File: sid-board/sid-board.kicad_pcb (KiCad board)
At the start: 2 copper layers, 13 parts, among them J1 ICM_CONN, J2 SID_CONN, J3 5V/GND, J4 3.3V/GND, J5 SPI, J6 UARTAB/IRQ, U1 SC16IS752IPW, U2 LM2596MODULE, U3 PCA82C250, U4 PCA82C250

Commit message: Happy with first prototype, going to try get it made!
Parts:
- J1, J2: footprint Connector_PinHeader_2.54mm:PinHeader_2x06_P2.54mm_Vertical -> sid-board:SAAB_SID_CONNECTOR_HEADER
- J3: value 5V/GND -> 5V OUT
- J4: value 3.3V/GND -> 3.3V IN
- J6: value UARTAB/IRQ -> UARTA/UARTB/IRQ
- U1: value SC16IS752IPW -> SC16IS752
- moved J3 14.3 mm to (92.6, 123.8)
- moved J6 14.2 mm to (81.2, 112.5)
- moved C2 12.2 mm to (87.0, 78.9), turned to 90 degrees
- moved U1 11.7 mm to (73.7, 112.4), turned to 180 degrees
- moved SPI 10.7 mm to (102.1, 123.4)
- moved J1 10.2 mm to (94.0, 66.0), turned to 0 degrees
- moved C1 9.02 mm to (80.0, 78.9), turned to 90 degrees
- moved U4 8.90 mm to (73.7, 76.2)
- moved R1 7.79 mm to (66.0, 108.3)
- moved J2 6.35 mm to (73.7, 66.0), turned to 0 degrees
- moved U2 5.08 mm to (83.8, 94.0)
- moved U3 4.84 mm to (93.3, 76.2)
- moved J4 4.27 mm to (83.8, 123.8)
- renumbered J5 to SPI
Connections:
- U3 pad 4: (no net) -> Net-(J6-Pad1)
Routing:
- net GND: track 0.00 -> 188.3 mm, vias 0 -> 3
- net VDD_5V: track 0.00 -> 78.5 mm, vias 0 -> 1
- net Net-(J6-Pad4): track 0.00 -> 64.5 mm
- net Net-(J6-Pad3): track 0.00 -> 61.5 mm
- net Net-(J6-Pad2): track 0.00 -> 49.5 mm, vias 0 -> 2
- net Net-(J6-Pad1): track 0.00 -> 45.9 mm, vias 0 -> 2
- net Net-(J5-Pad1): track 0.00 -> 41.9 mm
- net Net-(J6-Pad5): track 0.00 -> 41.2 mm
- net Net-(J5-Pad2): track 0.00 -> 39.2 mm
- net Net-(J5-Pad3): track 0.00 -> 37.2 mm
- net Net-(J5-Pad4): track 0.00 -> 35.1 mm
- net VDD_3.3V: track 0.00 -> 27.5 mm, vias 0 -> 2
- net VIN: track 0.00 -> 23.8 mm
- net Net-(J1-Pad6): track 0.00 -> 21.3 mm
- net Net-(J1-Pad3): track 0.00 -> 21.3 mm
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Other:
- board outline added: 42.8 x 68.8 mm
- board text added: "/// DESCRIPTION Provides an SPI breakout to a DUAL-UART interface, allowing for REVERSE-ENGINEERING of the SAAB SID/HPD. Designed for SAAB 9-3 Second Generation models (2003+), with high position SID. /// APPLICATION 1. Unplug SID. 2. Plug SID cable into ICM port (J1). 3. Connect SID to SID port (J2) via appropriate 12-core cable. 4. Interface to SPI bus with appropriate microcontroller."
- board text added: "/// SAAB SID /// INTERFACE"
- board text added: "3.3V"
- board text added: "5.0V"
- board text added: "GND"
- board text added: "ICM TO UART_A"
- board text added: "MISO"
- board text added: "MOSI"
- board text added: "RXA"
- board text added: "RXB"
- board text added: "SAAB SID INTERFACE LEIGH OLIVER 01/2020"
- board text added: "SCK"
- board text added: "SID TO UART_B"
- board text added: "TXA"
- board text added: "TXB"
- board text added: "~CS"
- board text added: "~IRQ"

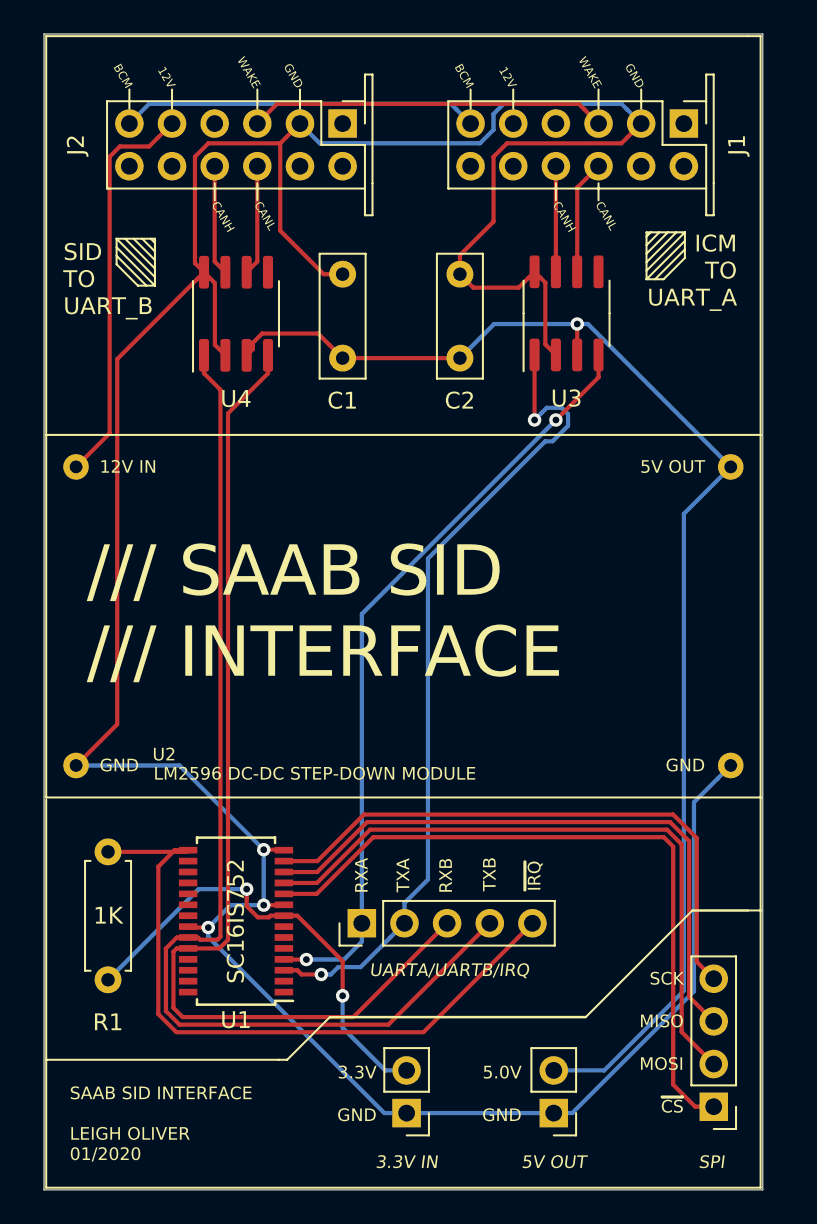
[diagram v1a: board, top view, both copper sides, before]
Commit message: Removed unnessecary cap, re-arranged.
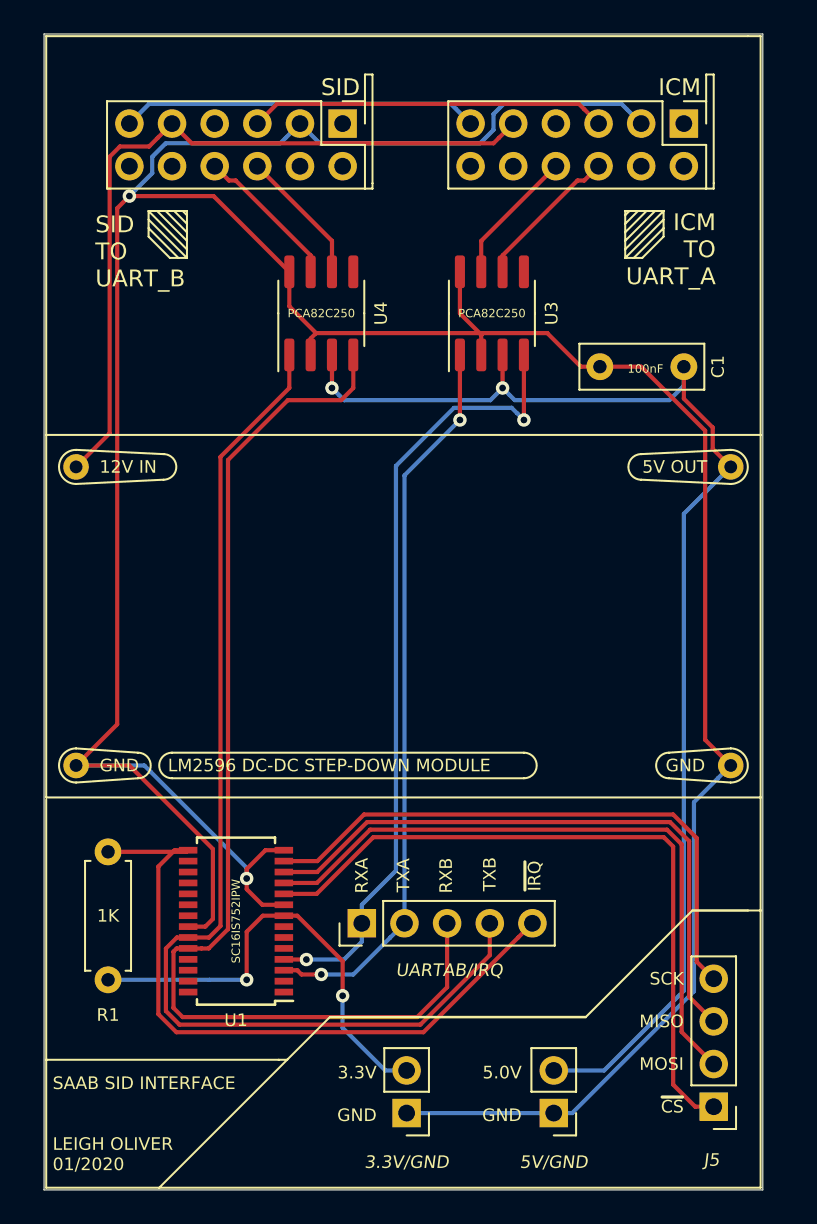
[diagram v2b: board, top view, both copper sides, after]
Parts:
- removed C2: 100nF, Capacitor_THT:C_Rect_L7.2mm_W2.5mm_P5.00mm_FKS2_FKP2_MKS2_MKP2
- J3: value 5V OUT -> 5V/GND
- J4: value 3.3V IN -> 3.3V/GND
- J6: value UARTA/UARTB/IRQ -> UARTAB/IRQ
- U1: value SC16IS752 -> SC16IS752IPW
- moved C1 20.3 mm to (100.3, 79.4), turned to 180 degrees
- moved U4 5.08 mm to (78.7, 76.2)
- moved U3 4.44 mm to (88.9, 76.2)
- renumbered SPI to J5
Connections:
- J1 pad 1: (no net) -> Net-(J1-Pad1)
- J1 pad 11: (no net) -> Net-(J1-Pad11)
- J1 pad 12: (no net) -> Net-(J1-Pad12)
- J1 pad 4: (no net) -> Net-(J1-Pad4)
- J1 pad 7: (no net) -> Net-(J1-Pad7)
- J1 pad 8: (no net) -> Net-(J1-Pad8)
- J2 pad 1: (no net) -> Net-(J2-Pad1)
- J2 pad 11: (no net) -> Net-(J2-Pad11)
- J2 pad 12: (no net) -> Net-(J2-Pad12)
- J2 pad 4: (no net) -> Net-(J2-Pad4)
- J2 pad 7: (no net) -> Net-(J2-Pad7)
- J2 pad 8: (no net) -> Net-(J2-Pad8)
- U1 pad 1: (no net) -> Net-(U1-Pad1)
- U1 pad 16: (no net) -> Net-(U1-Pad16)
- U1 pad 17: (no net) -> Net-(U1-Pad17)
- U1 pad 18: (no net) -> Net-(U1-Pad18)
- U1 pad 19: (no net) -> Net-(U1-Pad19)
- U1 pad 2: (no net) -> Net-(U1-Pad2)
- U1 pad 20: (no net) -> Net-(U1-Pad20)
- U1 pad 21: (no net) -> Net-(U1-Pad21)
- U1 pad 25: (no net) -> Net-(U1-Pad25)
- U1 pad 26: (no net) -> Net-(U1-Pad26)
- U1 pad 27: (no net) -> Net-(U1-Pad27)
- U1 pad 28: (no net) -> Net-(U1-Pad28)
- U1 pad 5: (no net) -> Net-(U1-Pad5)
- U1 pad 6: (no net) -> Net-(U1-Pad6)
- U1 pad 7: (no net) -> Net-(U1-Pad7)
- U3 pad 5: (no net) -> Net-(U3-Pad5)
- U4 pad 5: (no net) -> Net-(U4-Pad5)
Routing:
- net GND: track 188.3 -> 209.9 mm, vias 3 -> 2
- net VIN: track 23.8 -> 45.1 mm
- net Net-(J6-Pad3): track 61.5 -> 67.4 mm
- net Net-(J6-Pad2): track 49.5 -> 43.8 mm
- net Net-(J2-Pad9): track 6.58 -> 8.89 mm
- net Net-(J1-Pad10): track 6.81 -> 8.89 mm
- net VDD_5V: track 78.5 -> 76.5 mm, vias 1 -> 2
- net Net-(J6-Pad4): track 64.5 -> 66.5 mm
- net Net-(J1-Pad9): track 6.29 -> 8.13 mm
- net Net-(J6-Pad1): track 45.9 -> 47.5 mm
- net Net-(J2-Pad10): track 6.58 -> 8.13 mm
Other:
- board text added: "ICM"
- board text added: "SID"
- board text removed: "/// DESCRIPTION Provides an SPI breakout to a DUAL-UART interface, allowing for REVERSE-ENGINEERING of the SAAB SID/HPD. Designed for SAAB 9-3 Second Generation models (2003+), with high position SID. /// APPLICATION 1. Unplug SID. 2. Plug SID cable into ICM port (J1). 3. Connect SID to SID port (J2) via appropriate 12-core cable. 4. Interface to SPI bus with appropriate microcontroller."
- board text removed: "/// SAAB SID /// INTERFACE"

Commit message: Working on new mostly-SMD version, switched to independant LDOs, added oscillator circuit.
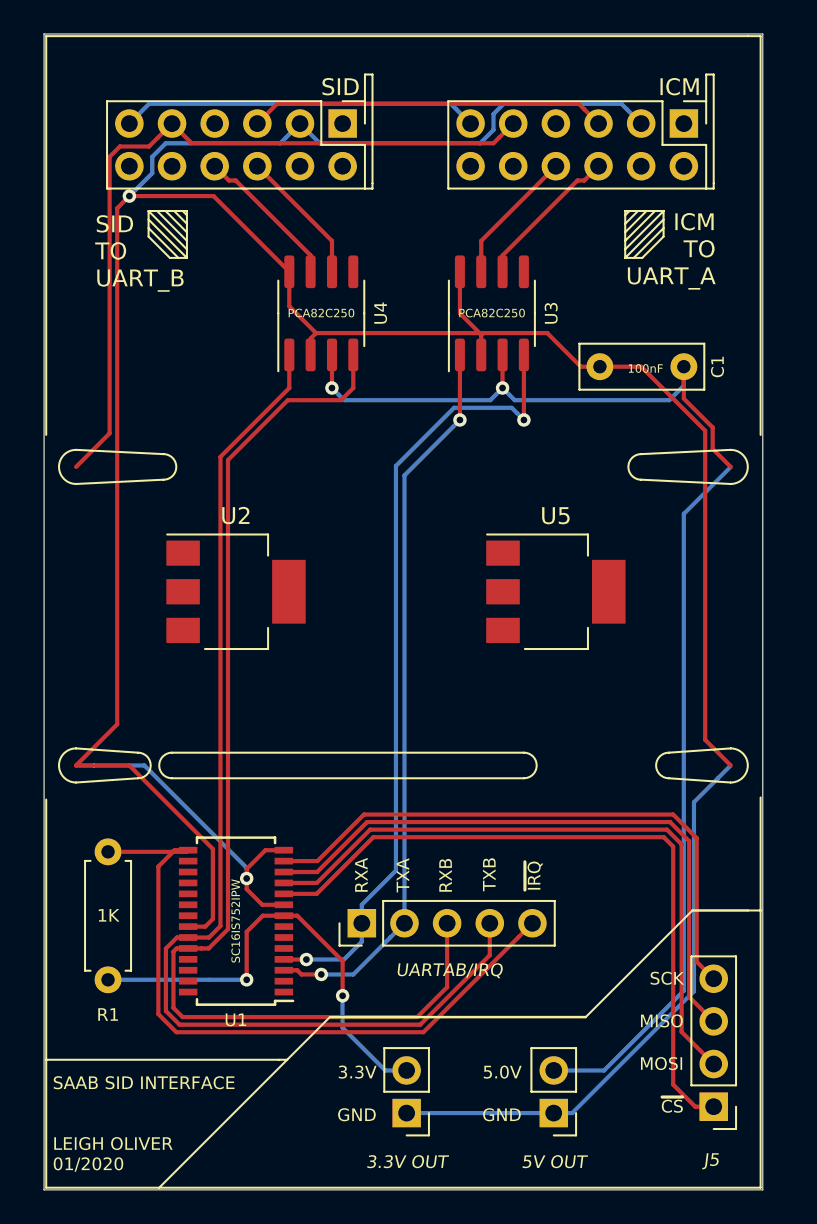
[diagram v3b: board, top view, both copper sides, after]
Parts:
- added U5: MCP1703A-5002_SOT223, Package_TO_SOT_SMD:SOT-223-3_TabPin2, F.Cu at (92.7, 92.8)
- J3: value 5V/GND -> 5V OUT
- J4: value 3.3V/GND -> 3.3V OUT
- U2: value LM2596MODULE -> MCP1703A-3302_SOT223; footprint sid-board:LM2596-MODULE -> Package_TO_SOT_SMD:SOT-223-3_TabPin2
- moved U2 10.2 mm to (73.7, 92.8)
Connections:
- net Net-(U1-Pad6) renamed XTAL1
- net Net-(U1-Pad7) renamed XTAL2
- U2 pad 3: VDD_5V -> VDD_3.3V
